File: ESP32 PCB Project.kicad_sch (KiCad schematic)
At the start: 5 parts, among them J1 SS-52400-002, U1 MCP73871

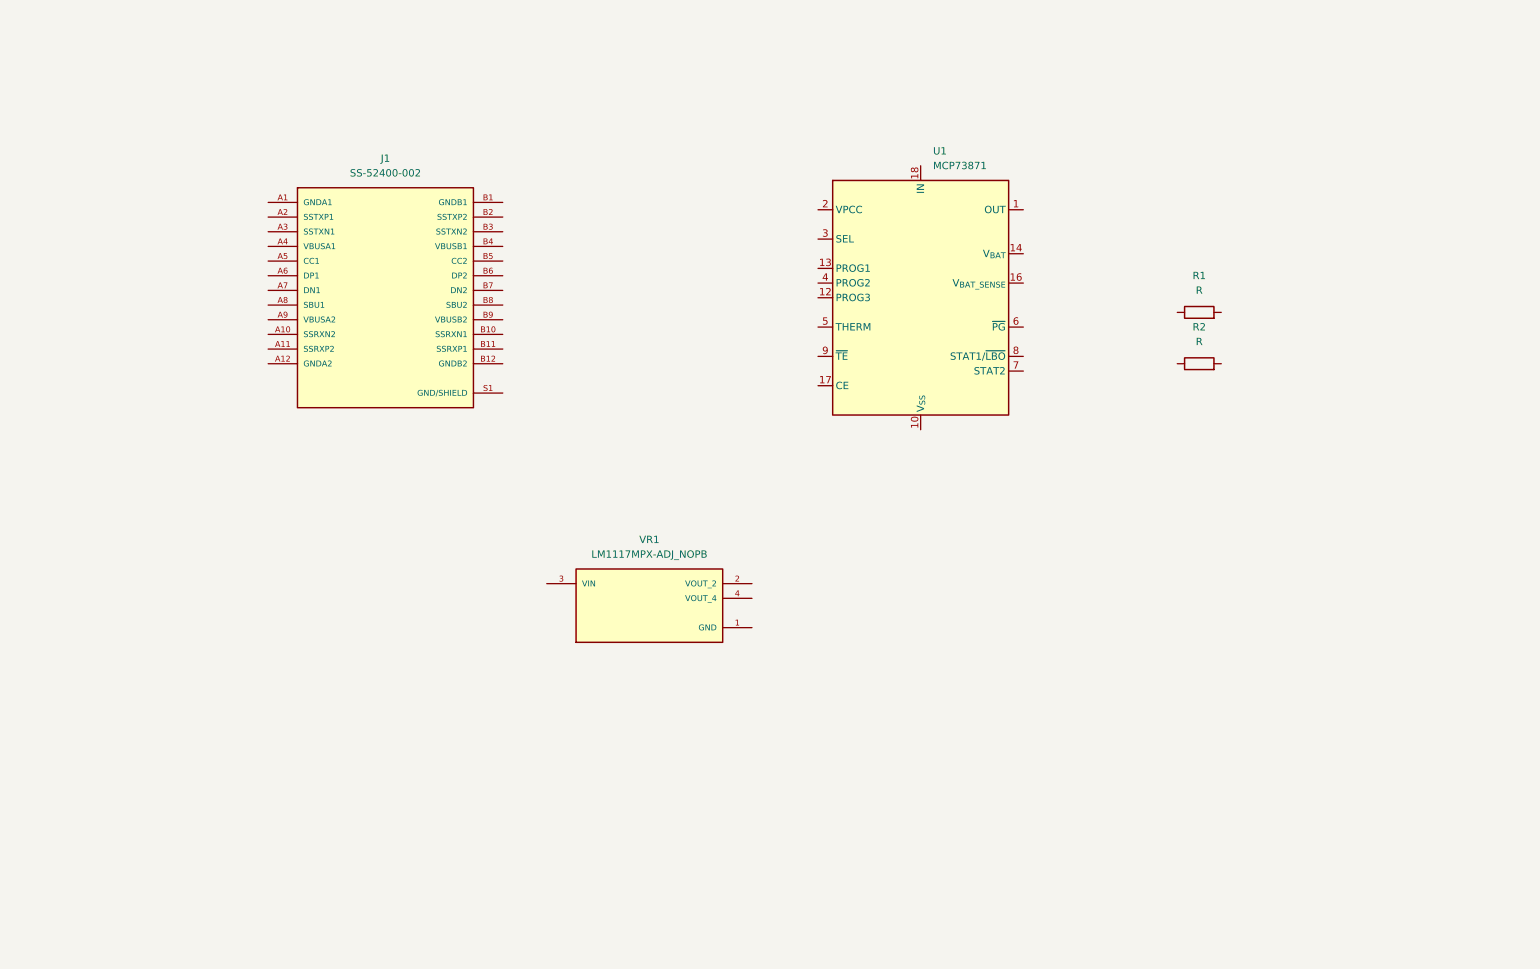
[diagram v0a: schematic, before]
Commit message: Add LiPo charging circuit to schematic
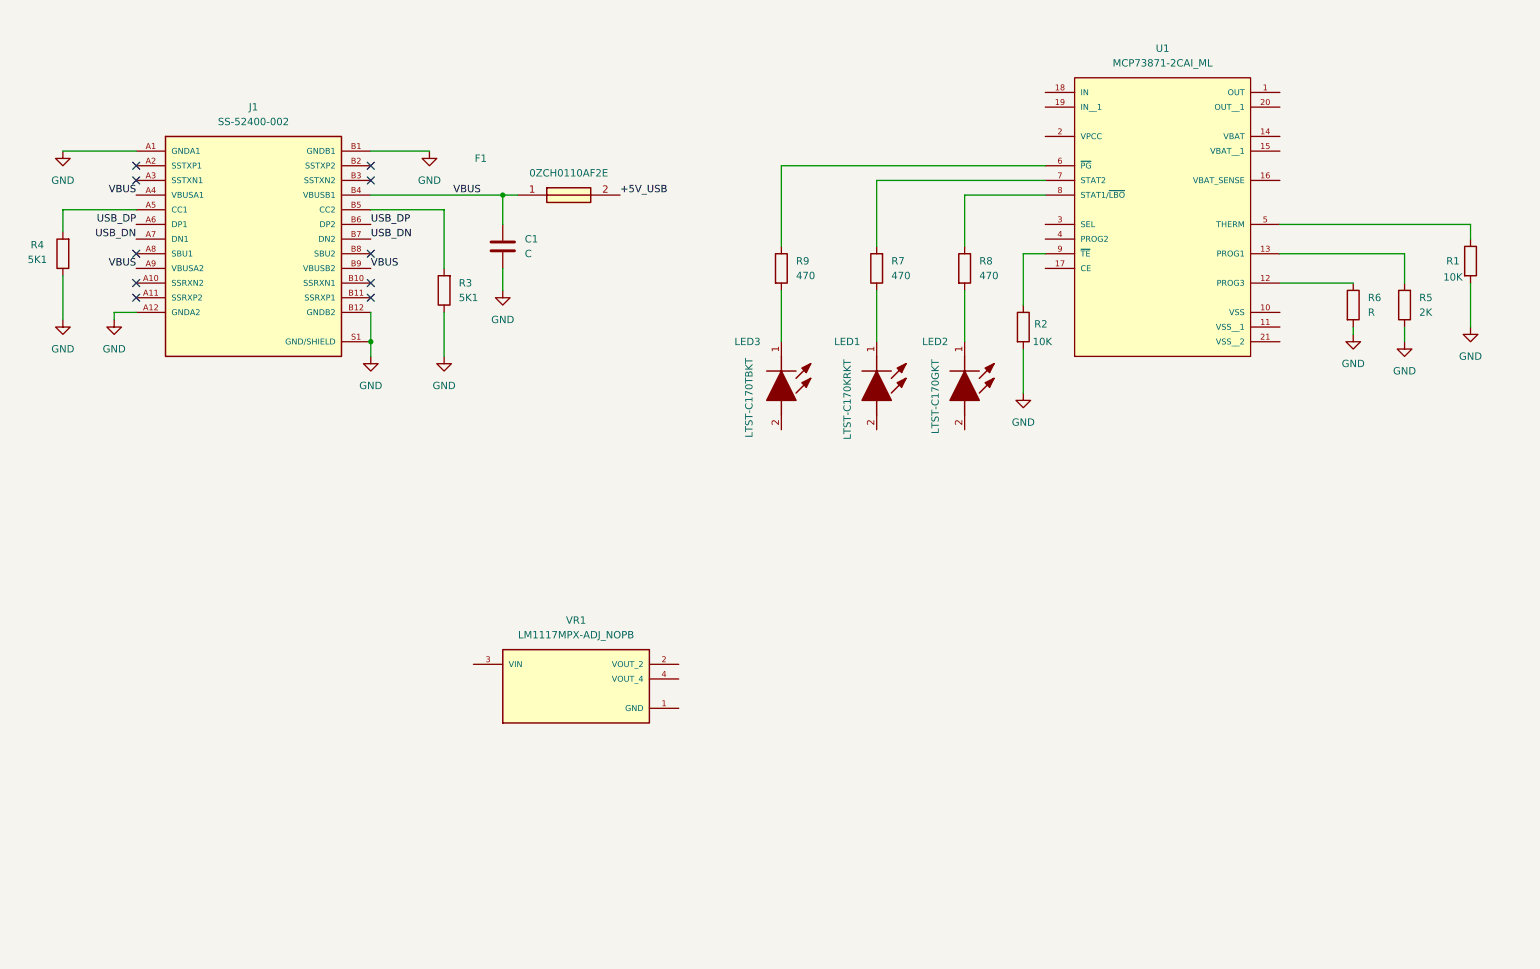
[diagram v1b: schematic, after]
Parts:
- removed U1: MCP73871, Package_DFN_QFN:QFN-20-1EP_4x4mm_P0.5mm_EP2.5x2.5mm, symbol Battery_Management:MCP73871
- added C1: C, symbol Device:C
- added F1: 0ZCH0110AF2E, FUSC3226X100N, symbol _.ESP32_symbols:0ZCH0110AF2E
- added LED1: LTST-C170KRKT, LEDC2012X120N, symbol _.ESP32_symbols:LTST-C170KRKT
- added LED2: LTST-C170GKT, LEDC2012X120N, symbol _.ESP32_symbols:LTST-C170GKT
- added LED3: LTST-C170TBKT, LEDC2012X120N, symbol _.ESP32_symbols:LTST-C170TBKT
- added R3, R4: 5K1, symbol Device:R
- added R5: 2K, symbol Device:R
- added R6: R, symbol Device:R
- added R7, R8, R9: 470, symbol Device:R
- added U1: MCP73871-2CAI_ML, MCP73871-2CAI_ML:QFN50P400X400X100-21N, symbol _.ESP32_symbols:MCP73871-2CAI_ML
- R1, R2: value R -> 10K
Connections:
- net at R1.1: now also U1.5 (THERM)
- net GND: now reaches R1.2
- net GND: now also J1.A1 (GNDA1), J1.A12 (GNDA2), J1.B1 (GNDB1), J1.B12 (GNDB2), J1.S1 (GND/SHIELD), R2.2, C1.2, R3.1, R4.1, R5.1, R6.2
- net at R2.1: now also U1.9 (~{TE})
- net VBUS: now reaches J1.A4 (VBUSA1)
- net VBUS: now also J1.A9 (VBUSA2), J1.B4 (VBUSB1), J1.B9 (VBUSB2), C1.1, F1.1
- net at J1.A5 (CC1): now also R4.2
- net USB_DP: now reaches J1.A6 (DP1)
- net USB_DP: now also J1.B6 (DP2)
- net USB_DN: now reaches J1.A7 (DN1)
- net USB_DN: now also J1.B7 (DN2)
- net at J1.B5 (CC2): now also R3.2
- new net: R6.1, U1.12 (PROG3)
- new net: R5.2, U1.13 (PROG1)
- new net: R9.1, U1.6 (~{PG})
- new net: R7.2, U1.7 (STAT2)
- new net: R8.1, U1.8 (STAT1/~{LBO})
- new net: LED2.1 (K), R8.2
- new net: LED1.1 (K), R7.1
- new net: LED3.1 (K), R9.2
- new net +5V_USB: F1.2
- no-connect marks 0 -> 10
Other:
- moved on the sheet: J1, R1, R2, VR1

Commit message: Add battery connector to schematic
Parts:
- added C2, C5: 0.1uF, symbol Device:C
- added C3, C4: 10uF, symbol Device:C_Polarized
- added C6: 1uF, symbol Device:C
- added J2: B2B-PH-SM4-TB, B2B-PH-SM4-TB:JST_B2B-PH-SM4-TB, symbol _.ESP32_symbols:B2B-PH-SM4-TB
- added LED4: LTST-C170KRKT, LEDC2012X120N, symbol _.ESP32_symbols:LTST-C170KRKT
- added R10: 470, symbol Device:R
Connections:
- net +5V_USB: now also LED1.2 (A), LED2.2 (A), LED3.2 (A), U1.17 (CE), U1.18 (IN), U1.19 (IN__1), U1.2 (VPCC), U1.4 (PROG2), C6.1
- net GND: now also U1.10 (VSS), U1.11 (VSS__1), U1.21 (VSS__2), U1.3 (SEL), VR1.1 (GND), C2.2, C3.2, C4.2, C5.2, C6.2, J2.1, R10.2
- net +5V: now reaches U1.1 (OUT)
- net +5V: now also U1.20 (OUT__1), VR1.3 (VIN), C2.1, C3.1
- net VBAT: now reaches U1.14 (VBAT)
- net VBAT: now also U1.15 (VBAT__1), U1.16 (VBAT_SENSE), J2.2
- net +3.3V: now reaches VR1.2 (VOUT_2)
- net +3.3V: now also VR1.4 (VOUT_4), C4.1, C5.1, LED4.2 (A)
- new net: LED4.1 (K), R10.1
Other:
- moved on the sheet: LED1, LED2, LED3, R1, R2, R5, R6, R7, R8, R9, U1, VR1
